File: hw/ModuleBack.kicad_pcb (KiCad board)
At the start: 2 copper layers, 48.3 x 99.1 mm, 77 parts, among them J16 mid_to_back_1, J17 mid_to_back_2, J18 power_bus, Q2 2SC1815, Q3 2SC1815, Q4 2SC1815, Q5 2SC1815, Q6 2SC1815, Q7 2SC1815, Q8 2SC1815, Q9 2SC1815, U10 LM2950G-3.3, U7 TL074, U8 TL074, U9 TL072

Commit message: Software: appended polarity selection functionality. Hardware: appended power reversal protection.           adjusted silks.
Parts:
- added D22: 1N5819, Diode_THT:D_DO-41_SOD81_P2.54mm_Vertical_AnodeUp, F.Cu at (110.5, 129.5)
- added D23: 1N5819, Diode_THT:D_DO-41_SOD81_P2.54mm_Vertical_AnodeUp, F.Cu at (120.7, 137.2)
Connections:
- J18 pad 1: -12V -> Net-(D22-Pad1)
- J18 pad 10: +12V -> Net-(D23-Pad2)
- J18 pad 2: -12V -> Net-(D22-Pad1)
- J18 pad 9: +12V -> Net-(D23-Pad2)
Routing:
- net +12V: track 217.8 -> 225.3 mm
- net Net-(D22-Pad1): track 0.00 -> 6.39 mm
- net Net-(D23-Pad2): track 0.00 -> 6.35 mm

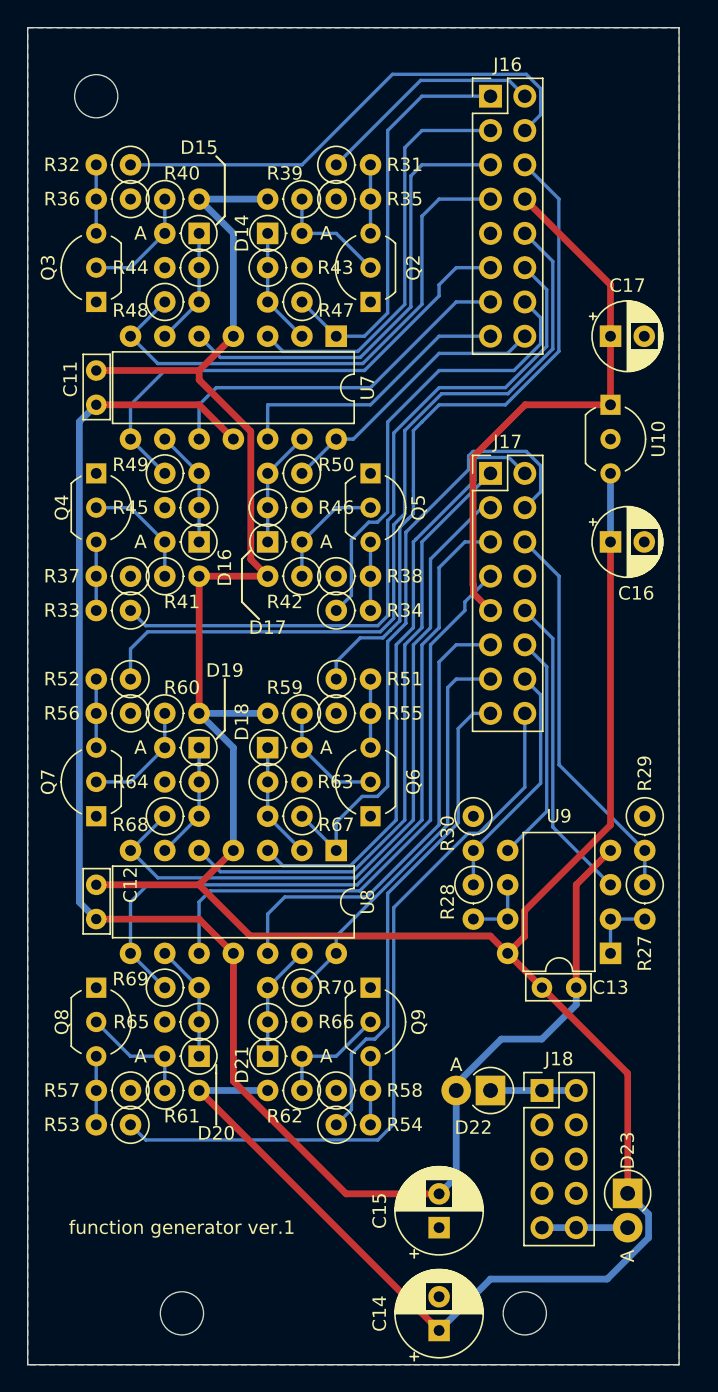
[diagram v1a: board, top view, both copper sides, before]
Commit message: Software: - Added CV control, but for limited functions. - Added BPM mode.
Hardware:
- Version ordered to Elecrow.
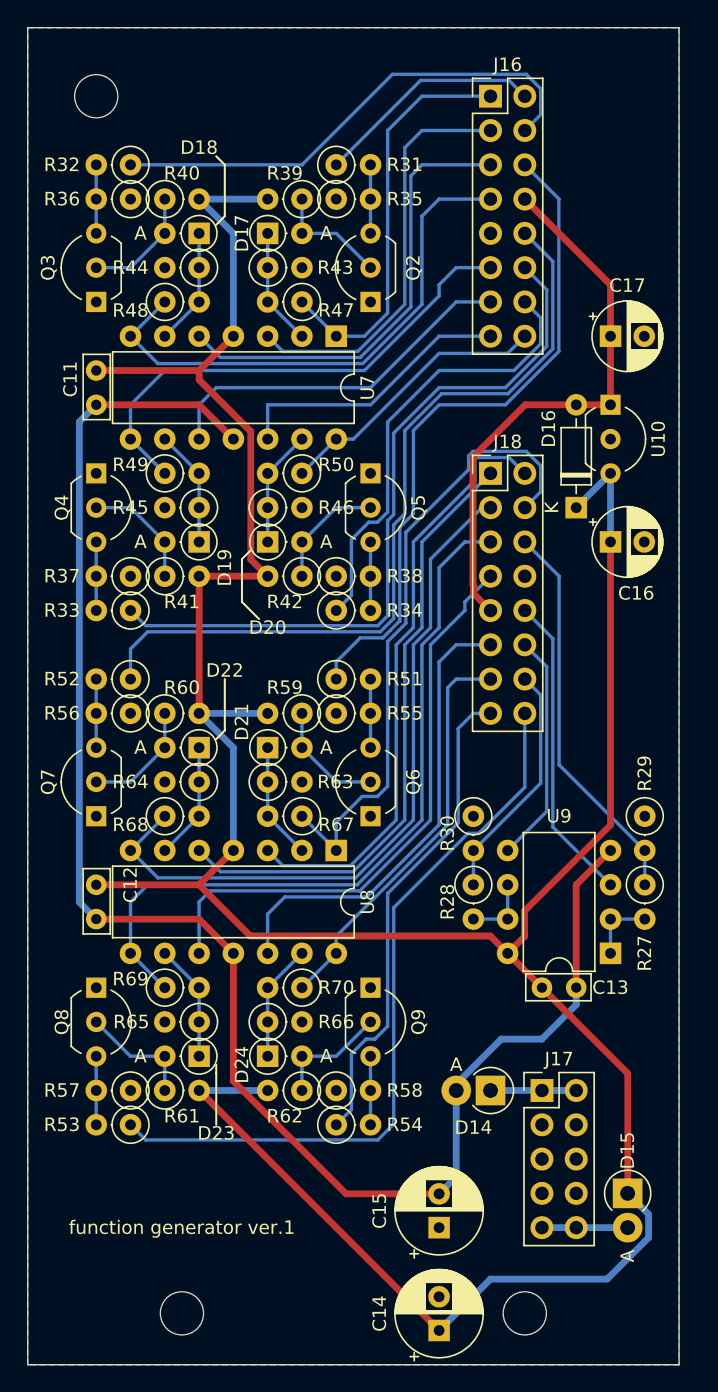
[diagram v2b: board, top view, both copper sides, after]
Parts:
- added D16: BAT48JFILM, Diode_THT:D_DO-35_SOD27_P7.62mm_Horizontal, F.Cu at (116.8, 86.4)
- renumbered D22 to D14, D23 to D15, D14 to D17, D15 to D18, D16 to D19, D17 to D20, D18 to D21, D19 to D22, D20 to D23, D21 to D24, J18 to J17, J17 to J18
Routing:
- net +12V: track 225.3 -> 228.8 mm
